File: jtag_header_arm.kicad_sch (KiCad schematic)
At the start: 7 parts, among them J5 02x10_2.54mm_Header_Odd_Even

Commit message: 1: adding JTAG header sheet name
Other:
- title: (none) -> STM32 JTAG Header
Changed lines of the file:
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@@
 	(paper "A4")
 	(title_block
+		(title "STM32 JTAG Header")
 		(date "2025-12-14")
 		(rev "rev A")
 		(company "Kebag-logic <contact@kebag-logic.com>")
+		(comment 1 "Condidential")
 	)
 	(text "ARM JTAG Header"

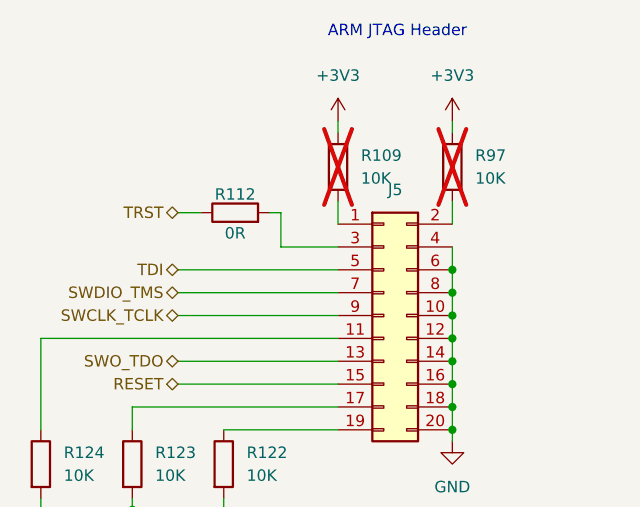
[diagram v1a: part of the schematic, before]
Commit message: updates symbols and fixes ERC errors. Refs: #9
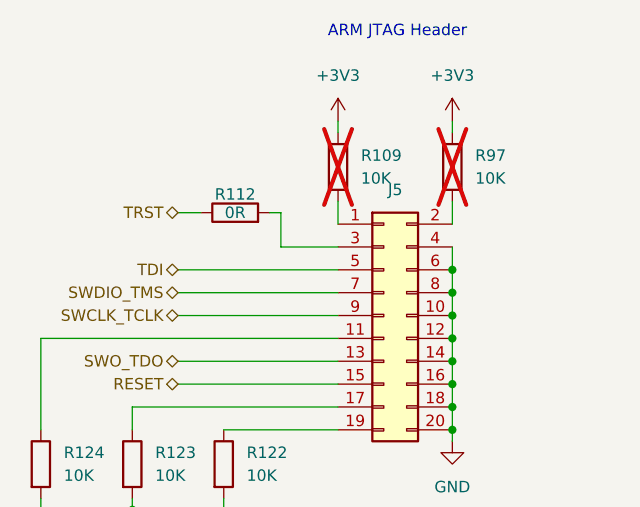
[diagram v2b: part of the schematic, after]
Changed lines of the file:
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@@
 		)
 		(property "Value" "0R"
-			(at 115.57 64.516 90)
+			(at 115.57 62.23 90)
 			(effects
 				(font
@@
 		(property "Package (in)" "2512"
 			(at 115.57 62.23 0)
-			(effects
-				(font
-					(size 1.27 1.27)
-				)
-				(hide yes)
-			)
-		)
-		(property "Dielectric" ""
-			(at 115.57 62.23 90)
-			(effects
-				(font
-					(size 1.27 1.27)
-				)
-				(hide yes)
-			)
-		)
-		(property "Dielectric_type" ""
-			(at 115.57 62.23 90)
-			(effects
-				(font
-					(size 1.27 1.27)
-				)
-				(hide yes)
-			)
-		)
-		(property "LSCS" ""
-			(at 115.57 62.23 90)
-			(effects
-				(font
-					(size 1.27 1.27)
-				)
-				(hide yes)
-			)
-		)
-		(property "Max Current" ""
-			(at 115.57 62.23 90)
 			(effects
 				(font
@@
 			)
 		)
-		(property "Dielectric" ""
-			(at 104.14 90.17 0)
-			(effects
-				(font
-					(size 1.27 1.27)
-				)
-				(hide yes)
-			)
-		)
-		(property "Dielectric_type" ""
-			(at 104.14 90.17 0)
-			(effects
-				(font
-					(size 1.27 1.27)
-				)
-				(hide yes)
-			)
-		)
-		(property "LSCS" ""
-			(at 104.14 90.17 0)
-			(effects
-				(font
-					(size 1.27 1.27)
-				)
-				(hide yes)
-			)
-		)
-		(property "Max Current" ""
-			(at 104.14 90.17 0)
-			(effects
-				(font
-					(size 1.27 1.27)
-				)
-				(hide yes)
-			)
-		)
 		(pin "1"
 		)
@@
 			)
 		)
-		(property "Dielectric" ""
-			(at 93.98 90.17 0)
-			(effects
-				(font
-					(size 1.27 1.27)
-				)
-				(hide yes)
-			)
-		)
-		(property "Dielectric_type" ""
-			(at 93.98 90.17 0)
-			(effects
-				(font
-					(size 1.27 1.27)
-				)
-				(hide yes)
-			)
-		)
-		(property "LSCS" ""
-			(at 93.98 90.17 0)
-			(effects
-				(font
-					(size 1.27 1.27)
-				)
-				(hide yes)
-			)
-		)
-		(property "Max Current" ""
-			(at 93.98 90.17 0)
-			(effects
-				(font
-					(size 1.27 1.27)
-				)
-				(hide yes)
-			)
-		)
 		(pin "1"
 		)
@@
 			)
 		)
-		(property "Dielectric" ""
-			(at 127 57.15 0)
-			(effects
-				(font
-					(size 1.27 1.27)
-				)
-				(hide yes)
-			)
-		)
-		(property "Dielectric_type" ""
-			(at 127 57.15 0)
-			(effects
-				(font
-					(size 1.27 1.27)
-				)
-				(hide yes)
-			)
-		)
-		(property "LSCS" ""
-			(at 127 57.15 0)
-			(effects
-				(font
-					(size 1.27 1.27)
-				)
-				(hide yes)
-			)
-		)
-		(property "Max Current" ""
-			(at 127 57.15 0)
-			(effects
-				(font
-					(size 1.27 1.27)
-				)
-				(hide yes)
-			)
-		)
 		(pin "1"
 		)
@@
 			)
 		)
-		(property "Dielectric" ""
-			(at 114.3 90.17 0)
-			(effects
-				(font
-					(size 1.27 1.27)
-				)
-				(hide yes)
-			)
-		)
-		(property "Dielectric_type" ""
-			(at 114.3 90.17 0)
-			(effects
-				(font
-					(size 1.27 1.27)
-				)
-				(hide yes)
-			)
-		)
-		(property "LSCS" ""
-			(at 114.3 90.17 0)
-			(effects
-				(font
-					(size 1.27 1.27)
-				)
-				(hide yes)
-			)
-		)
-		(property "Max Current" ""
-			(at 114.3 90.17 0)
-			(effects
-				(font
-					(size 1.27 1.27)
-				)
-				(hide yes)
-			)
-		)
 		(pin "1"
 		)
@@
 			(at 139.7 57.15 0)
 			(effects
-				(font
-					(size 1.27 1.27)
-				)
-				(hide yes)
-			)
-		)
-		(property "Dielectric" ""
-			(at 139.7 57.15 0)
-			(effects
-				(font
-					(size 1.27 1.27)
-				)
-				(hide yes)
-			)
-		)
-		(property "Dielectric_type" ""
-			(at 139.7 57.15 0)
-			(effects
-				(font
-					(size 1.27 1.27)
-				)
-				(hide yes)
-			)
-		)
-		(property "LSCS" ""
-			(at 139.7 57.15 0)
-			(effects
-				(font
-					(size 1.27 1.27)
-				)
-				(hide yes)
-			)
-		)
-		(property "Max Current" ""
-			(at 139.7 57.15 0)
-			(effects

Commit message: updates 0R resistor to 0603. Refs: #31
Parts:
- R112: footprint KL_Footprints:R_2512 -> KL_Footprints:R_0603; symbol KL_R:R_0R_2W_5_2512 -> KL_R:R_0R_100mW_5_0603; Digikey 118-CRF2512-J/-000ELFCT-ND -> YAG1307CT-ND; LCSC C2778666 -> C3017805; Mouser 652-CRF2512-J-000ELF -> 603-RC0603JR-070RP; Package (in) 2512 -> 0603; Power 2 -> 0.1
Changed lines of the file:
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@@
 	)
 	(symbol
-		(lib_id "KL_R:R_0R_2W_5_2512")
+		(lib_id "KL_R:R_0R_100mW_5_0603")
 		(at 115.57 62.23 90)
 		(unit 1)
@@
 			)
 		)
-		(property "Footprint" "KL_Footprints:R_2512"
+		(property "Footprint" "KL_Footprints:R_0603"
 			(at 115.57 64.008 90)
 			(effects
@@
 			)
 		)
-		(property "Datasheet" "~"
+		(property "Datasheet" "https://yageogroup.com/component-documentation/download/specsheet/RC0603JR-070RP"
 			(at 115.57 62.23 0)
 			(effects
@@
 			)
 		)
-		(property "Power" "2"
+		(property "Power" "0.1"
 			(at 115.57 62.23 0)
 			(effects
@@
 			)
 		)
-		(property "Mouser" "652-CRF2512-J-000ELF "
+		(property "Mouser" "603-RC0603JR-070RP"
 			(at 115.57 62.23 0)
 			(effects
@@
 			)
 		)
-		(property "Digikey" "118-CRF2512-J/-000ELFCT-ND"
+		(property "Digikey" "YAG1307CT-ND"
 			(at 115.57 62.23 0)
 			(effects
@@
 			)
 		)
-		(property "LCSC" "C2778666"
+		(property "LCSC" "C3017805"
 			(at 115.57 62.23 0)
 			(effects
@@
 			)
 		)
-		(property "Package (in)" "2512"
+		(property "Package (in)" "0603"
 			(at 115.57 62.23 0)
 			(effects

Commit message: updates jtag_header_arm. Refs: #41
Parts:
- J5: value 02x10_2.54mm_Header_Odd_Even -> Header_10x02_2.54mm_2.54mm_Straight; symbol KL_Headers:02x10_2.54mm_Header_Odd_Even -> KL_Header:Header_10x02_2.54mm_2.54mm_Straight; MPN (none) -> BHR-20-VUA; No_of_pins (none) -> 10; No_of_rows (none) -> 2; Orientation (none) -> Straight; Pitch_pin_in_mm (none) -> 2.54; Pitch_row_in_mm (none) -> 2.54
- R109, R122, R123, R124, R97: symbol KL_R:R_10K_100mW_5_0603 -> KL_R:R_10K_0.1W_5pct_0603; MPN (none) -> CRCW060310K0JNEC; Package (in) 0603 -> (none); Package_in_inch (none) -> 0603; Power 100mW -> (none); Power_in_W (none) -> 0.1; Tolerance 5% -> (none); Tolerance_in_pct (none) -> 5
- R112: symbol KL_R:R_0R_100mW_5_0603 -> KL_R:R_0R_0.1W_5pct_0603; MPN (none) -> RC0603JR-070RP; Package (in) 0603 -> (none); Package_in_inch (none) -> 0603; Power 0.1 -> (none); Power_in_W (none) -> 0.1; Tolerance 5 -> (none); Tolerance_in_pct (none) -> 5

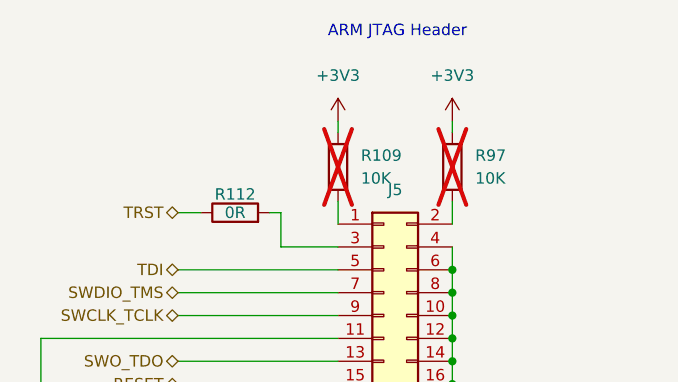
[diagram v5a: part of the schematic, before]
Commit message: moves all STM32 power behind the 0R resistor. Refs: #57
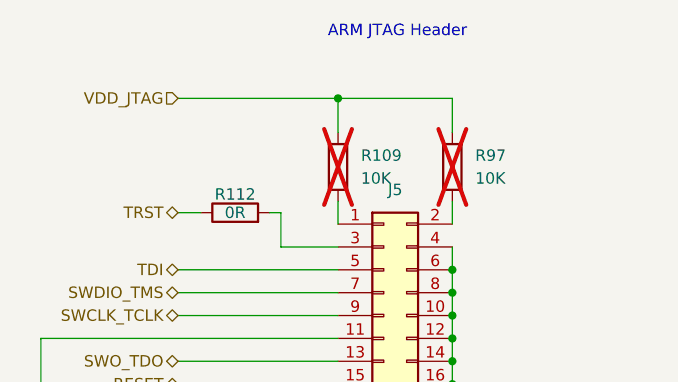
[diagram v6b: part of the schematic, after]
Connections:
- net +3V3 renamed VDD_JTAG
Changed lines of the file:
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@@
+	)
+	(junction
+		(at 127 49.53)
+		(diameter 0)
+		(color 0 0 0 0)
 	)
 	(junction
@@
 	(wire
 		(pts
+			(xy 127 49.53) (xy 139.7 49.53)
+		)
+		(stroke
+			(width 0)
+			(type default)
+		)
+	)
+	(wire
+		(pts
 			(xy 104.14 96.52) (xy 104.14 95.25)
 		)
@@
 	(wire
 		(pts
-			(xy 139.7 52.07) (xy 139.7 53.34)
-		)
-		(stroke
-			(width 0)
-			(type default)
-		)
-	)
-	(wire
-		(pts
 			(xy 139.7 66.04) (xy 139.7 68.58)
 		)
@@
 	(wire
 		(pts
+			(xy 109.22 49.53) (xy 127 49.53)
+		)
+		(stroke
+			(width 0)
+			(type default)
+		)
+	)
+	(wire
+		(pts
+			(xy 139.7 49.53) (xy 139.7 53.34)
+		)
+		(stroke
+			(width 0)
+			(type default)
+		)
+	)
+	(wire
+		(pts
 			(xy 139.7 73.66) (xy 139.7 76.2)
 		)
@@
 	(wire
 		(pts
-			(xy 127 52.07) (xy 127 53.34)
-		)
-		(stroke
-			(width 0)
-			(type default)
-		)
-	)
-	(wire
-		(pts
 			(xy 109.22 81.28) (xy 127 81.28)
 		)
@@
 		(pts
 			(xy 139.7 60.96) (xy 139.7 63.5)
+		)
+		(stroke
+			(width 0)
+			(type default)
+		)
+	)
+	(wire
+		(pts
+			(xy 127 49.53) (xy 127 53.34)
 		)
 		(stroke
@@
 		)
 	)
+	(hierarchical_label "VDD_JTAG"
+		(shape input)
+		(at 109.22 49.53 180)
+		(effects
+			(font
+				(size 1.27 1.27)
+			)
+			(justify right)
+		)
+	)
 	(symbol
 		(lib_id "KL_R:R_0R_0.1W_5pct_0603")
@@
 					(unit 1)
 				)
-			)
-		)
-	)
-	(symbol
-		(lib_id "power:+3V3")
-		(at 127 52.07 0)
-		(unit 1)
-		(body_style 1)
-		(exclude_from_sim no)
-		(in_bom yes)
-		(on_board yes)
-		(in_pos_files yes)
-		(dnp no)
-		(fields_autoplaced yes)
-		(property "Reference" "#PWR78"
-			(at 127 55.88 0)
-			(hide yes)
-			(show_name no)
-			(do_not_autoplace no)
-			(effects
-				(font
-					(size 1.27 1.27)
-				)
-			)
-		)
-		(property "Value" "+3V3"
-			(at 127 46.99 0)
-			(show_name no)
-			(do_not_autoplace no)
-			(effects
-				(font
-					(size 1.27 1.27)
-				)
-			)
-		)
-		(property "Footprint" ""
-			(at 127 52.07 0)
-			(hide yes)
-			(show_name no)
-			(do_not_autoplace no)
-			(effects
-				(font
-					(size 1.27 1.27)
-				)
-			)
-		)
-		(property "Datasheet" ""
-			(at 127 52.07 0)
-			(hide yes)
-			(show_name no)
-			(do_not_autoplace no)
-			(effects
-				(font
-					(size 1.27 1.27)
-				)
-			)
-		)
-		(property "Description" "Power symbol creates a global label with name \"+3V3\""
-			(at 127 52.07 0)
-			(hide yes)
-			(show_name no)
-			(do_not_autoplace no)
-			(effects
-				(font
-					(size 1.27 1.27)
-				)
-			)
-		)
-		(pin "1"
-		)
-		(instances
-			(project "shish-lan"
-				(path "/d4536448-b109-4159-96e2-3dc21baf2d6e/06488c82-a47f-4277-b0ee-3bd211d8922a/54dd0313-e11b-4c5a-bb43-942dea0cd180"
-					(reference "#PWR78")
-					(unit 1)
-				)
-			)
-		)
-	)
-	(symbol
-		(lib_id "power:+3V3")
-		(at 139.7 52.07 0)
-		(unit 1)
-		(body_style 1)
-		(exclude_from_sim no)
-		(in_bom yes)
-		(on_board yes)
-		(in_pos_files yes)
-		(dnp no)
-		(fields_autoplaced yes)
-		(property "Reference" "#PWR79"
-			(at 139.7 55.88 0)
-			(hide yes)
-			(show_name no)
-			(do_not_autoplace no)
-			(effects
-				(font
-					(size 1.27 1.27)
-				)
-			)
-		)
-		(property "Value" "+3V3"
-			(at 139.7 46.99 0)
-			(show_name no)
-			(do_not_autoplace no)
-			(effects
-				(font
-					(size 1.27 1.27)
-				)
-			)
-		)
-		(property "Footprint" ""
-			(at 139.7 52.07 0)
-			(hide yes)
-			(show_name no)
-			(do_not_autoplace no)
-			(effects
-				(font
-					(size 1.27 1.27)
-				)
-			)
-		)
-		(property "Datasheet" ""
-			(at 139.7 52.07 0)
-			(hide yes)
-			(show_name no)
-			(do_not_autoplace no)
-			(effects
-				(font
-					(size 1.27 1.27)
-				)
-			)
-		)
-		(property "Description" "Power symbol creates a global label with name \"+3V3\""
-			(at 139.7 52.07 0)
-			(hide yes)
-			(show_name no)
-			(do_not_autoplace no)
-			(effects
-				(font
-					(size 1.27 1.27)
-				)
-			)
-		)
-		(pin "1"
-		)
-		(instances
-			(project "shish-lan"
-				(path "/d4536448-b109-4159-96e2-3dc21baf2d6e/06488c82-a47f-4277-b0ee-3bd211d8922a/54dd0313-e11b-4c5a-bb43-942dea0cd180"
-					(reference "#PWR79")
-					(unit 1)
-				)
